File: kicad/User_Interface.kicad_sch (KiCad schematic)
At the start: 0 parts

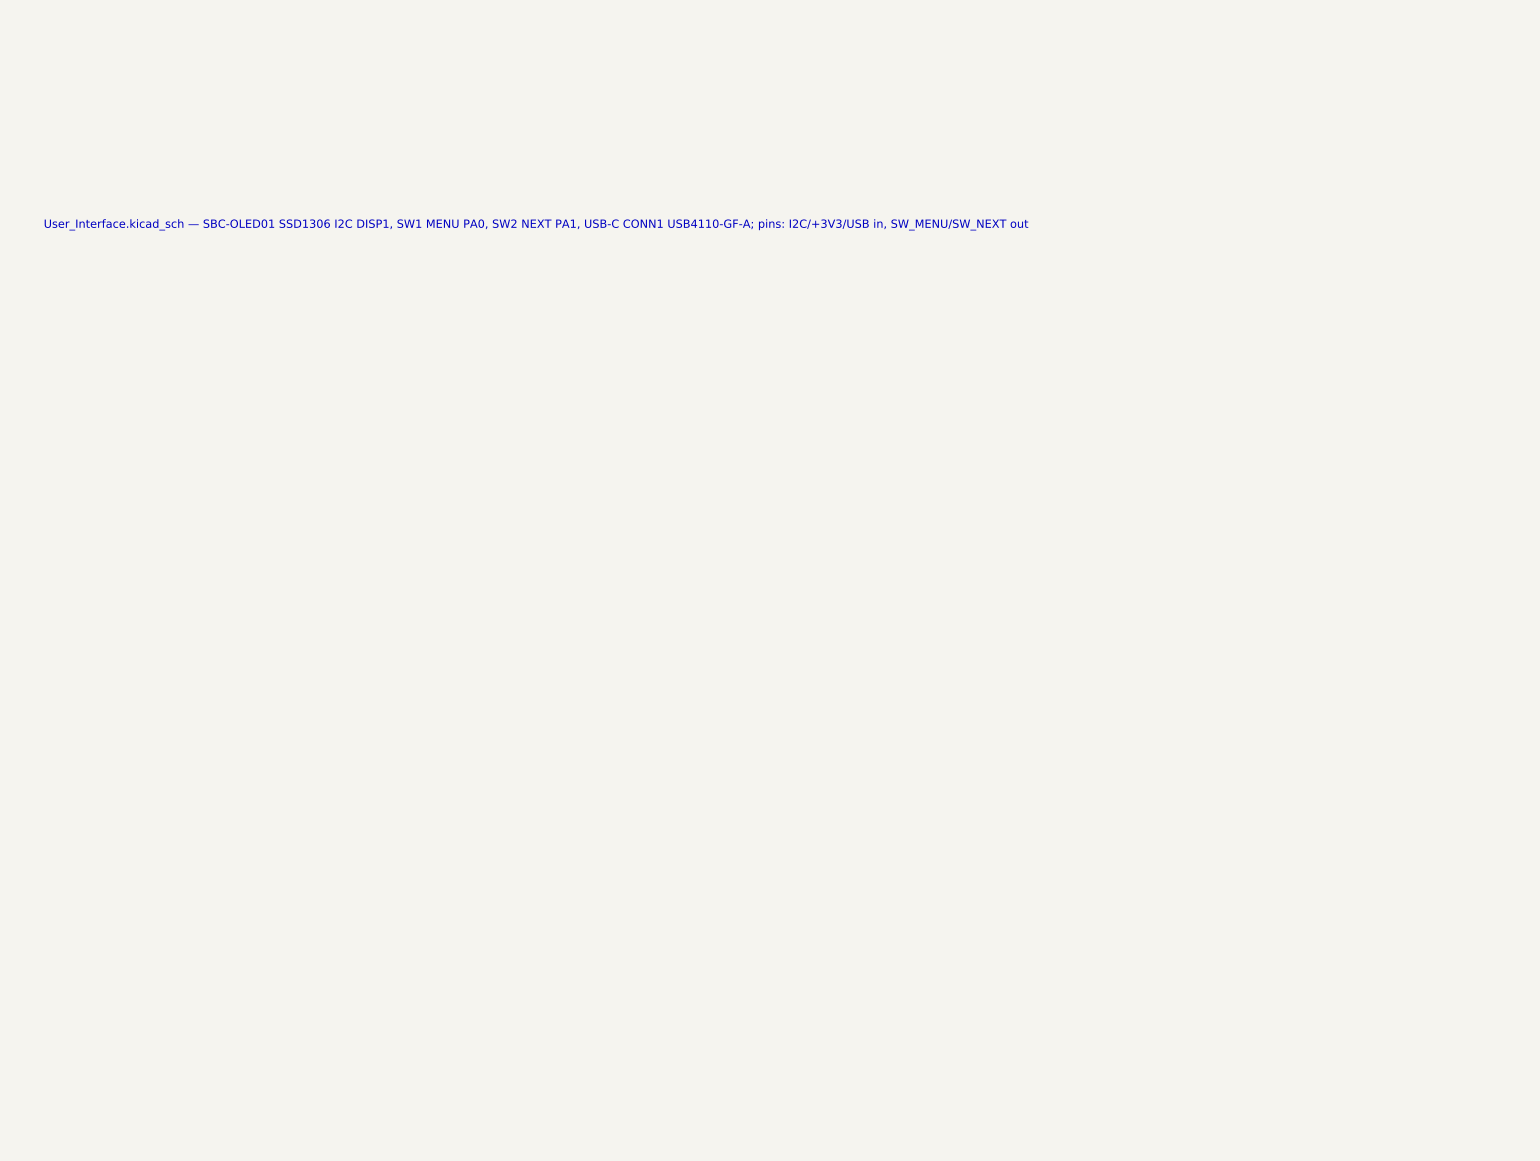
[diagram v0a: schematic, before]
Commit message: Add calibration scripts, documentation, simulation tools, and KiCad updates
- cal/calibration.py: 3-phase RF linearity calibration (29 freq, 28 power steps,
  1 MHz–10 GHz, direct generator→DUT, no attenuator, NRP sensor 0.01 dBm precision)
- cal/temp_calibration.py: temperature calibration via Vötsch chamber (16–40°C,
  Vötsch SIMSERV TCP driver, tracking generator source, outputs TEMP_COEFF_DB_PER_C[])
- cal/results/: dry-run calibration tables (.h/.json), figures, PDF reports
- doc/: ADC signal path analysis, calibration procedure (3-phase), lab optimisation
  guide updated for 1 MHz–10 GHz range and temperature correction firmware formula
- doc/diagrams/: PlantUML/Mermaid source + rendered PNGs for pipeline, firmware,
  and RF signal chain architectures
- sim/ltpwr_to_touchstone.py: LTpowerAnalyzer Z(f) → Touchstone S1P + Z1P via
  scikit-rf for SIwave PI-AC Decoupling Optimization DC/DC source impedance import
- sim/Measured_source_impedance.txt/.s1p/.z1p: DC/DC output impedance measurement
  and converted Touchstone files (100 Hz–10 MHz, 201 points)
- kicad/: updated schematics (MCU, power management, RF frontend, UI) and PCB layout
- kicad/fixture-rev_A/: test fixture DXF drawings
- lib/: Würth 744231091 datasheet, Hammond 1590A board outline footprint
- pp_3d_printer_setup_spec.md, pp_horn_antenna_manufacturing_spec.md: process specs

Co-Authored-By: Claude Sonnet 4.6 <noreply@anthropic.com>
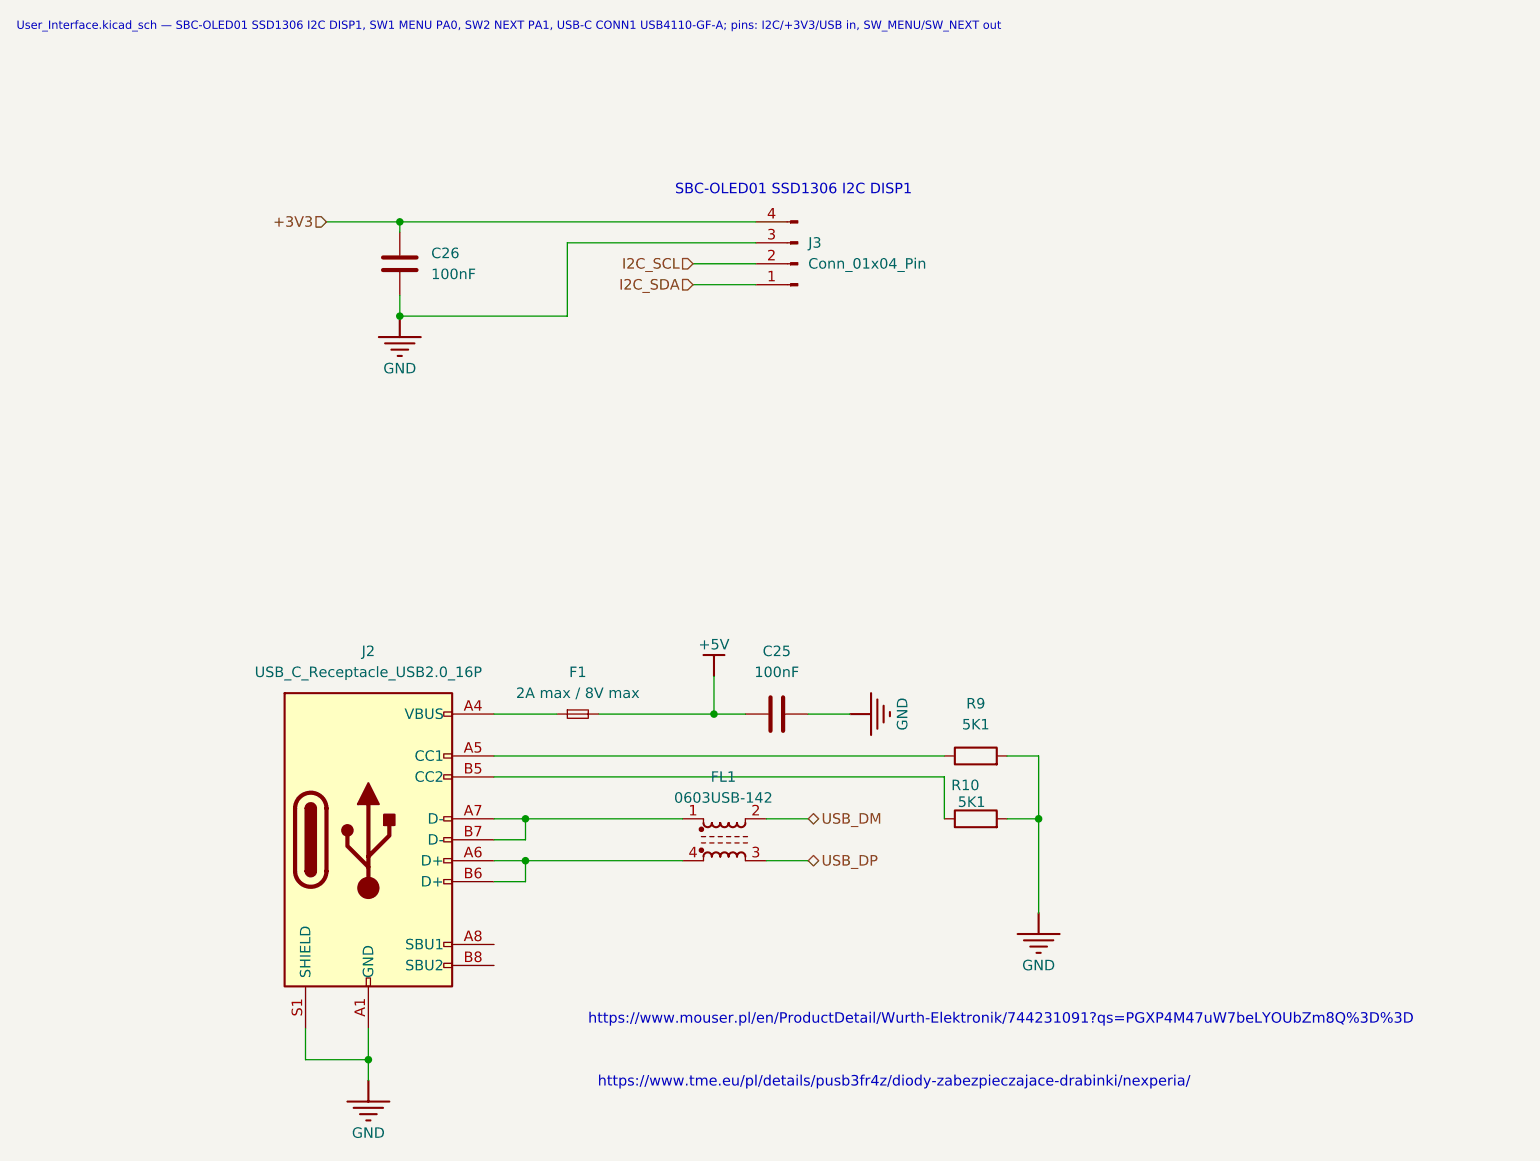
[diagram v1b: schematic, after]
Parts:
- added C25, C26: 100nF, Capacitor_SMD:C_0402_1005Metric, symbol Device:C
- added F1: 2A max / 8V max, Fuse:Fuse_1812_4532Metric_Pad1.30x3.40mm_HandSolder, symbol Device:Fuse_Small
- added FL1: 0603USB-142, Inductor_SMD:L_CommonModeChoke_Coilcraft_0603USB, symbol Filter:0603USB-142
- added J2: USB_C_Receptacle_USB2.0_16P, Connector_USB:USB_C_Receptacle_G-Switch_GT-USB-7010ASV, symbol Connector:USB_C_Receptacle_USB2.0_16P
- added J3: Conn_01x04_Pin, Connector_PinSocket_2.54mm:PinSocket_1x04_P2.54mm_Vertical, symbol Connector:Conn_01x04_Pin
- added R10, R9: 5K1, Resistor_SMD:R_0402_1005Metric_Pad0.72x0.64mm_HandSolder, symbol Device:R
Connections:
- new net: F1.1, J2.A4 (VBUS), J2.A9 (VBUS), J2.B4 (VBUS), J2.B9 (VBUS)
- new net: FL1.1, J2.A7 (D-), J2.B7 (D-)
- new net: FL1.4, J2.A6 (D+), J2.B6 (D+)
- new net: J2.B5 (CC2), R10.1
- new net: J2.A5 (CC1), R9.1
- new net +3V3: C26.2, J3.4 (Pin_4)
- new net +5V: C25.2, F1.2
- new net GND: C25.1, C26.1, J2.A1 (GND), J2.A12 (GND), J2.B1 (GND), J2.B12 (GND), J2.S1 (SHIELD), J3.3 (Pin_3), R10.2, R9.2
- new net I2C_SCL: J3.2 (Pin_2)
- new net I2C_SDA: J3.1 (Pin_1)
- new net USB_DM: FL1.2
- new net USB_DP: FL1.3
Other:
- note added: "SBC-OLED01 SSD1306 I2C DISP1"
- note added: "https://www.mouser.pl/en/ProductDetail/Wurth-Elektronik/744231091?qs=PGXP4M47uW7beLYOUbZm8Q%3D%3D"
- note added: "https://www.tme.eu/pl/details/pusb3fr4z/diody-zabezpieczajace-drabinki/nexperia/"
